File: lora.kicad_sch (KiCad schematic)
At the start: 30 parts, among them J13 Conn_Coaxial, Q14 2N7002, U12 E22P-915M30S

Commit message: assign lcsc part numbers
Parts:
- R101, R92, R94, R97: LCSC Part C2902636 -> C54951138
- U12: JLCPCB Part (none) -> C51912672; LCSC Part C51912672 -> (none)
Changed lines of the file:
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@@
 			)
 		)
-		(property "LCSC Part" "C2902636"
+		(property "LCSC Part" "C54951138"
 			(at 49.53 166.37 0)
 			(hide yes)
@@
 			)
 		)
-		(property "LCSC Part" "C2902636"
+		(property "LCSC Part" "C54951138"
 			(at 134.62 82.55 0)
 			(hide yes)
@@
 			)
 		)
-		(property "LCSC Part" "C51912672"
+		(property "JLCPCB Part" "C51912672"
 			(at 170.18 124.46 0)
 			(hide yes)
@@
 			)
 		)
-		(property "LCSC" ""
+		(property "KLC_S3.3" ""
 			(at 170.18 93.98 0)
 			(hide yes)
@@
 			)
 		)
-		(property "KLC_S3.3" ""
+		(property "KLC_S5.1" ""
 			(at 170.18 93.98 0)
 			(hide yes)
@@
 			)
 		)
-		(property "KLC_S5.1" ""
+		(property "Capacitor Rating" ""
 			(at 170.18 93.98 0)
 			(hide yes)
@@
 			)
 		)
-		(property "Capacitor Rating" ""
+		(property "LCSC Part" ""
 			(at 170.18 93.98 0)
 			(hide yes)
@@
 			)
 		)
-		(property "LCSC Part" "C2902636"
+		(property "LCSC Part" "C54951138"
 			(at 198.12 99.06 0)
 			(hide yes)
@@
 			)
 		)
-		(property "LCSC Part" "C2902636"
+		(property "LCSC Part" "C54951138"
 			(at 63.5 82.55 0)
 			(hide yes)

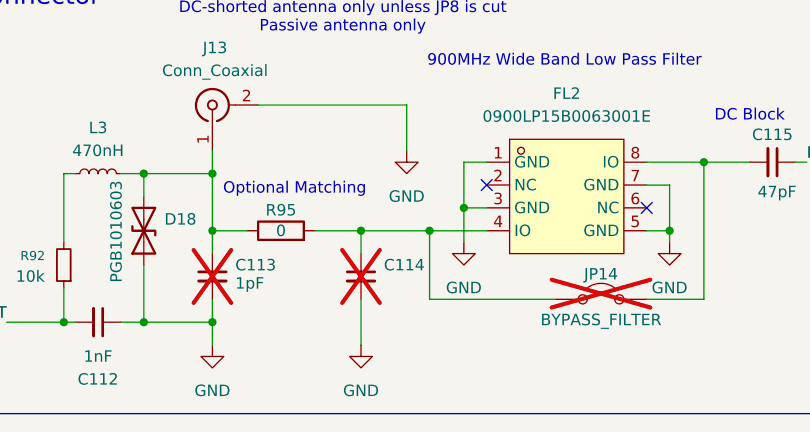
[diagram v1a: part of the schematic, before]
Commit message: new part numbers for out of stock components
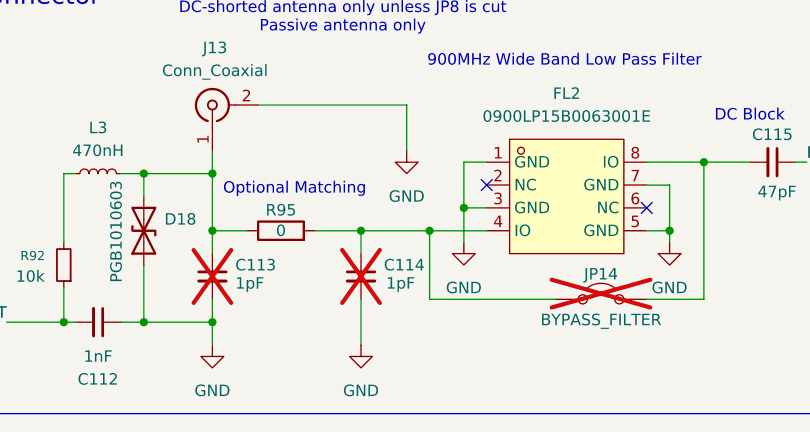
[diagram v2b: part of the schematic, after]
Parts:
- C113, C114: now left out of the parts list
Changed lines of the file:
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@@
 		(body_style 1)
 		(exclude_from_sim no)
-		(in_bom yes)
+		(in_bom no)
 		(on_board yes)
 		(in_pos_files yes)
@@
 		)
 		(property "Value" "1pF"
-			(at 71.882 170.942 0)
-			(hide yes)
+			(at 85.344 168.402 0)
 			(show_name no)
 			(do_not_autoplace no)
@@
 		(body_style 1)
 		(exclude_from_sim no)
-		(in_bom yes)
+		(in_bom no)
 		(on_board yes)
 		(in_pos_files yes)

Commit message: backup before switching to kicad-nightly
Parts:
- D18: footprint Capacitor_SMD:C_0603_1608Metric -> Diode_SMD:D_0603_1608Metric_Pad1.05x0.95mm_HandSolder
- J13: value Conn_Coaxial -> XUNPU SMA-KE-347-H13.5-1.6; LCSC Part C5250058 -> C5723200
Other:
- moved on the sheet: C116
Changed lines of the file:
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@@
 	(wire
 		(pts
+			(xy 134.62 91.44) (xy 134.62 88.9)
+		)
+		(stroke
+			(width 0)
+			(type default)
+		)
+	)
+	(wire
+		(pts
 			(xy 58.42 158.75) (xy 58.42 156.21)
 		)
@@
 	(wire
 		(pts
-			(xy 130.81 88.9) (xy 134.62 88.9)
+			(xy 128.27 88.9) (xy 134.62 88.9)
 		)
 		(stroke
@@
 	(wire
 		(pts
-			(xy 134.62 93.98) (xy 134.62 96.52)
-		)
-		(stroke
-			(width 0)
-			(type default)
-		)
-	)
-	(wire
-		(pts
 			(xy 58.42 172.72) (xy 66.04 172.72)
 		)
@@
 	(wire
 		(pts
+			(xy 134.62 97.79) (xy 134.62 96.52)
+		)
+		(stroke
+			(width 0)
+			(type default)
+		)
+	)
+	(wire
+		(pts
 			(xy 212.09 93.98) (xy 215.9 93.98)
 		)
@@
 	(hierarchical_label "RESET"
 		(shape input)
-		(at 130.81 88.9 180)
+		(at 128.27 88.9 180)
 		(effects
 			(font
@@
 	(symbol
 		(lib_id "power:GND")
-		(at 134.62 96.52 0)
+		(at 134.62 97.79 0)
 		(unit 1)
 		(body_style 1)
@@
 		(dnp no)
 		(property "Reference" "#PWR0128"
-			(at 134.62 102.87 0)
+			(at 134.62 104.14 0)
 			(hide yes)
 			(show_name no)
@@
 		)
 		(property "Value" "GND"
-			(at 134.62 100.838 0)
+			(at 134.62 102.108 0)
 			(show_name no)
 			(do_not_autoplace no)
@@
 		)
 		(property "Footprint" ""
-			(at 134.62 96.52 0)
+			(at 134.62 97.79 0)
 			(hide yes)
 			(show_name no)
@@
 		)
 		(property "Datasheet" ""
-			(at 134.62 96.52 0)
+			(at 134.62 97.79 0)
 			(hide yes)
 			(show_name no)
@@
 		)
 		(property "Description" "Power symbol creates a global label with name \"GND\" , ground"
-			(at 134.62 96.52 0)
+			(at 134.62 97.79 0)
 			(hide yes)
 			(show_name no)
@@
 		)
 		(property "Value" "22uF"
-			(at 197.612 79.756 0)
+			(at 197.866 83.058 0)
 			(show_name no)
 			(do_not_autoplace no)
@@
 			)
 		)
-		(property "Value" "Conn_Coaxial"
+		(property "Value" "XUNPU SMA-KE-347-H13.5-1.6"
 			(at 66.3332 144.78 90)
 			(show_name no)
@@
 			)
 		)
-		(property "LCSC Part" "C5250058"
+		(property "LCSC Part" "C5723200"
 			(at 66.04 148.59 0)
 			(hide yes)
@@
 			)
 		)
+		(property "Capacitor Rating" ""
+			(at 66.04 148.59 0)
+			(hide yes)
+			(show_name no)
+			(do_not_autoplace no)
+			(effects
+				(font
+					(size 1.27 1.27)
+				)
+			)
+		)
 		(pin "1"
 		)
@@
 			)
 		)
-		(property "Footprint" "Capacitor_SMD:C_0603_1608Metric"
+		(property "Footprint" "Diode_SMD:D_0603_1608Metric_Pad1.05x0.95mm_HandSolder"
 			(at 58.42 162.56 0)
 			(hide yes)
@@
 			)
 		)
+		(property "Capacitor Rating" ""
+			(at 58.42 162.56 0)
+			(hide yes)
+			(show_name no)
+			(do_not_autoplace no)
+			(effects
+				(font
+					(size 1.27 1.27)
+				)
+			)
+		)
 		(pin "2"
 		)
@@
 	(symbol
 		(lib_id "Device:C_Small")
-		(at 134.62 91.44 0)
+		(at 134.62 93.98 0)
 		(unit 1)
 		(body_style 1)
@@
 		(dnp no)
 		(property "Reference" "C116"
-			(at 130.556 91.44 0)
+			(at 131.318 92.202 0)
 			(show_name no)
 			(do_not_autoplace no)
@@
 		)
 		(property "Value" "100nF"
-			(at 130.302 93.98 0)
+			(at 131.064 96.52 0)
 			(show_name no)
 			(do_not_autoplace no)
@@
 		)
 		(property "Footprint" "Capacitor_SMD:C_0402_1005Metric"
-			(at 134.62 91.44 0)
+			(at 134.62 93.98 0)
 			(hide yes)
 			(show_name no)
@@
 		)
 		(property "Datasheet" ""
-			(at 134.62 91.44 0)
+			(at 134.62 93.98 0)
 			(hide yes)
 			(show_name no)
@@
 		)
 		(property "Description" "Unpolarized capacitor, small symbol"
-			(at 134.62 91.44 0)
+			(at 134.62 93.98 0)
 			(hide yes)
 			(show_name no)
@@
 		)
 		(property "LCSC Part" "C5272680"
-			(at 134.62 91.44 0)
+			(at 134.62 93.98 0)
 			(hide yes)
 			(show_name no)
@@
 		)
 		(property "Voltage Rating" "50V"
-			(at 134.62 91.44 0)
+			(at 134.62 93.98 0)
 			(hide yes)
 			(show_name no)
@@
 		)
 		(property "Tolerance" ""
-			(at 134.62 91.44 0)
+			(at 134.62 93.98 0)
 			(hide yes)
 			(show_name no)
@@
 		)
 		(property "LCSC" ""
-			(at 134.62 91.44 90)
+			(at 134.62 93.98 90)
 			(hide yes)
 			(show_name no)
@@
 		)
 		(property "KLC_S3.3" ""
-			(at 134.62 91.44 90)
+			(at 134.62 93.98 90)
 			(hide yes)
 			(show_name no)
@@
 		)
 		(property "KLC_S5.1" ""
-			(at 134.62 91.44 90)
+			(at 134.62 93.98 90)
 			(hide yes)
 			(show_name no)
@@
 		)
 		(property "Capacitor Rating" "X7R"
-			(at 134.62 91.44 0)
+			(at 134.62 93.98 0)
 			(hide yes)
 			(show_name no)

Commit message: organize part fields
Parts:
- C112: Dielectric (none) -> C0G; MPN (none) -> CC0402CG50V102JN; Manufacturer (none) -> TORCH; Tolerance (none) -> 5%; Voltage Rating (none) -> 50V
- C113, C114: Capacitor Rating C0G -> (none); Dielectric (none) -> C0G
- C115: Capacitor Rating C0G -> (none); Dielectric (none) -> C0G; MPN (none) -> CGA0402C0G470J500GT; Manufacturer (none) -> HRE; Tolerance (none) -> 5%; Voltage Rating 25V -> 50V
- C116, C121: Capacitor Rating X7R -> (none); Dielectric (none) -> X7R; MPN (none) -> 0402B104J500NT; Manufacturer (none) -> FH (Fenghua); Tolerance (none) -> 5%
- C117, C118: Dielectric (none) -> X5R; MPN (none) -> HGC0402R5105K500NTEJ; Manufacturer (none) -> Chinocera; Tolerance (none) -> 10%
- C119, C120: Dielectric (none) -> X5R; MPN (none) -> CL31A226KAHNNNE; Manufacturer (none) -> Samsung Electro-Mechanics; Tolerance (none) -> 10%
- D18: MPN (none) -> PGB1010603NR; Manufacturer (none) -> Littelfuse
- D19: MPN (none) -> TPD1E10B06DPYR; Manufacturer (none) -> Texas Instruments
- FL2: Manufacturer JOHANSON(约翰逊) -> Johanson Technology
- J13: value XUNPU SMA-KE-347-H13.5-1.6 -> SMA-KE-347-H13.5-1.6; MPN (none) -> SMA-KE-347-H13.5-1.6; Manufacturer (none) -> XUNPU
- L3: MPN (none) -> LQW18ANR47G00D; Manufacturer (none) -> Murata; Tolerance (none) -> 2%
- Q14: MPN (none) -> 2N7002; Manufacturer (none) -> MSKSEMI
- R100: MPN (none) -> 0805W8F0000T5E; Manufacturer (none) -> UNI-ROYAL
- R101, R92, R94, R97: MPN (none) -> FRH0402D1002TS; Manufacturer (none) -> FOJAN; Power Rating (none) -> 62.5mW; Tolerance (none) -> 0.5%
- R102: MPN (none) -> WF04H1004BTL; Manufacturer (none) -> Walsin; Power Rating (none) -> 100mW; Tolerance (none) -> 0.1%
- R93, R95: MPN (none) -> CRCW04020000Z0EDHP; Manufacturer (none) -> Vishay
- R96: MPN (none) -> ARG02BTC1003; Manufacturer (none) -> Viking Tech; Power Rating (none) -> 62.5mW; Tolerance (none) -> 0.1%
- R98: MPN (none) -> ARG02DTC0220; Manufacturer (none) -> Viking Tech; Power Rating (none) -> 62.5mW; Tolerance (none) -> 0.5%
- R99: MPN (none) -> FRH0402B1001TS; Manufacturer (none) -> FOJAN; Power Rating (none) -> 62.5mW; Tolerance (none) -> 0.1%
- U12: JLCPCB Part C51912672 -> (none); LCSC Part (none) -> C51912672; Manufacturer EBYTE(亿佰特) -> Ebyte
